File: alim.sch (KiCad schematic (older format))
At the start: 22 parts, among them IC10 74LS138, IC11 74LS138, IC12 74LS139, IC2 74LS09, IC5 74LS123, IC6 74LS393, IC7 74LS14, IC8 74LS04, IC9 74LS11

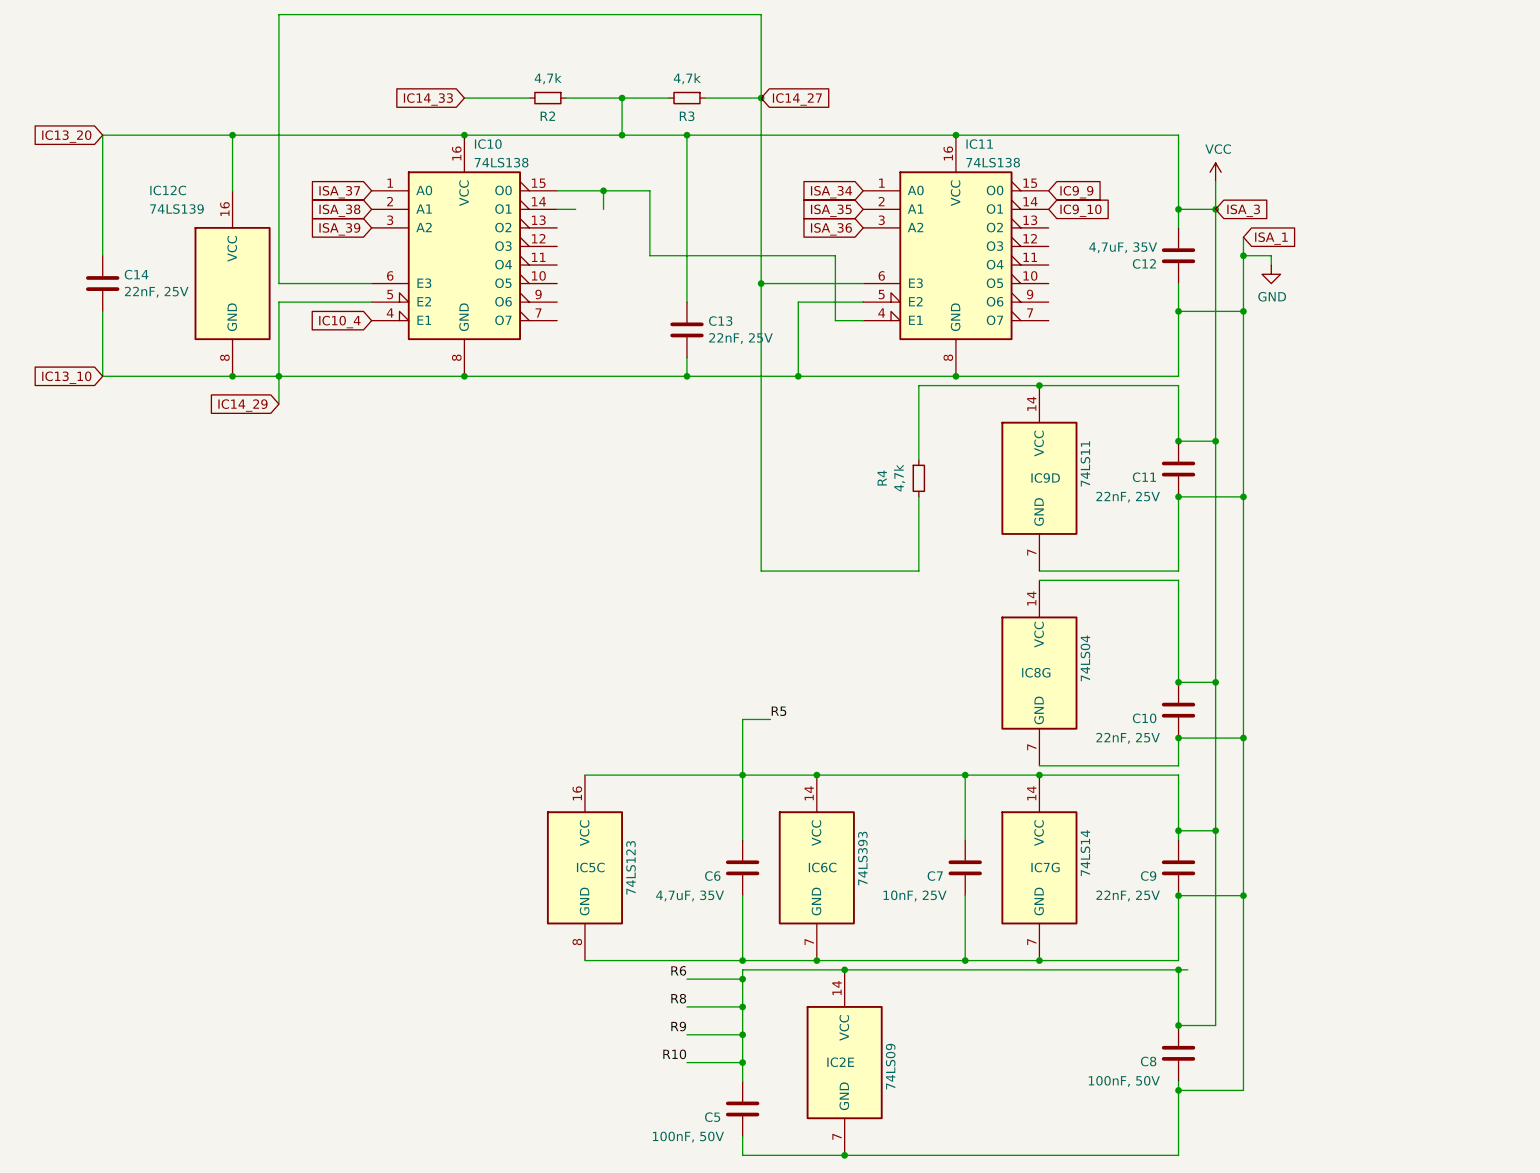
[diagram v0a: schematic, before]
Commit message: modification du bus ISA. ajout de nom sur les pads
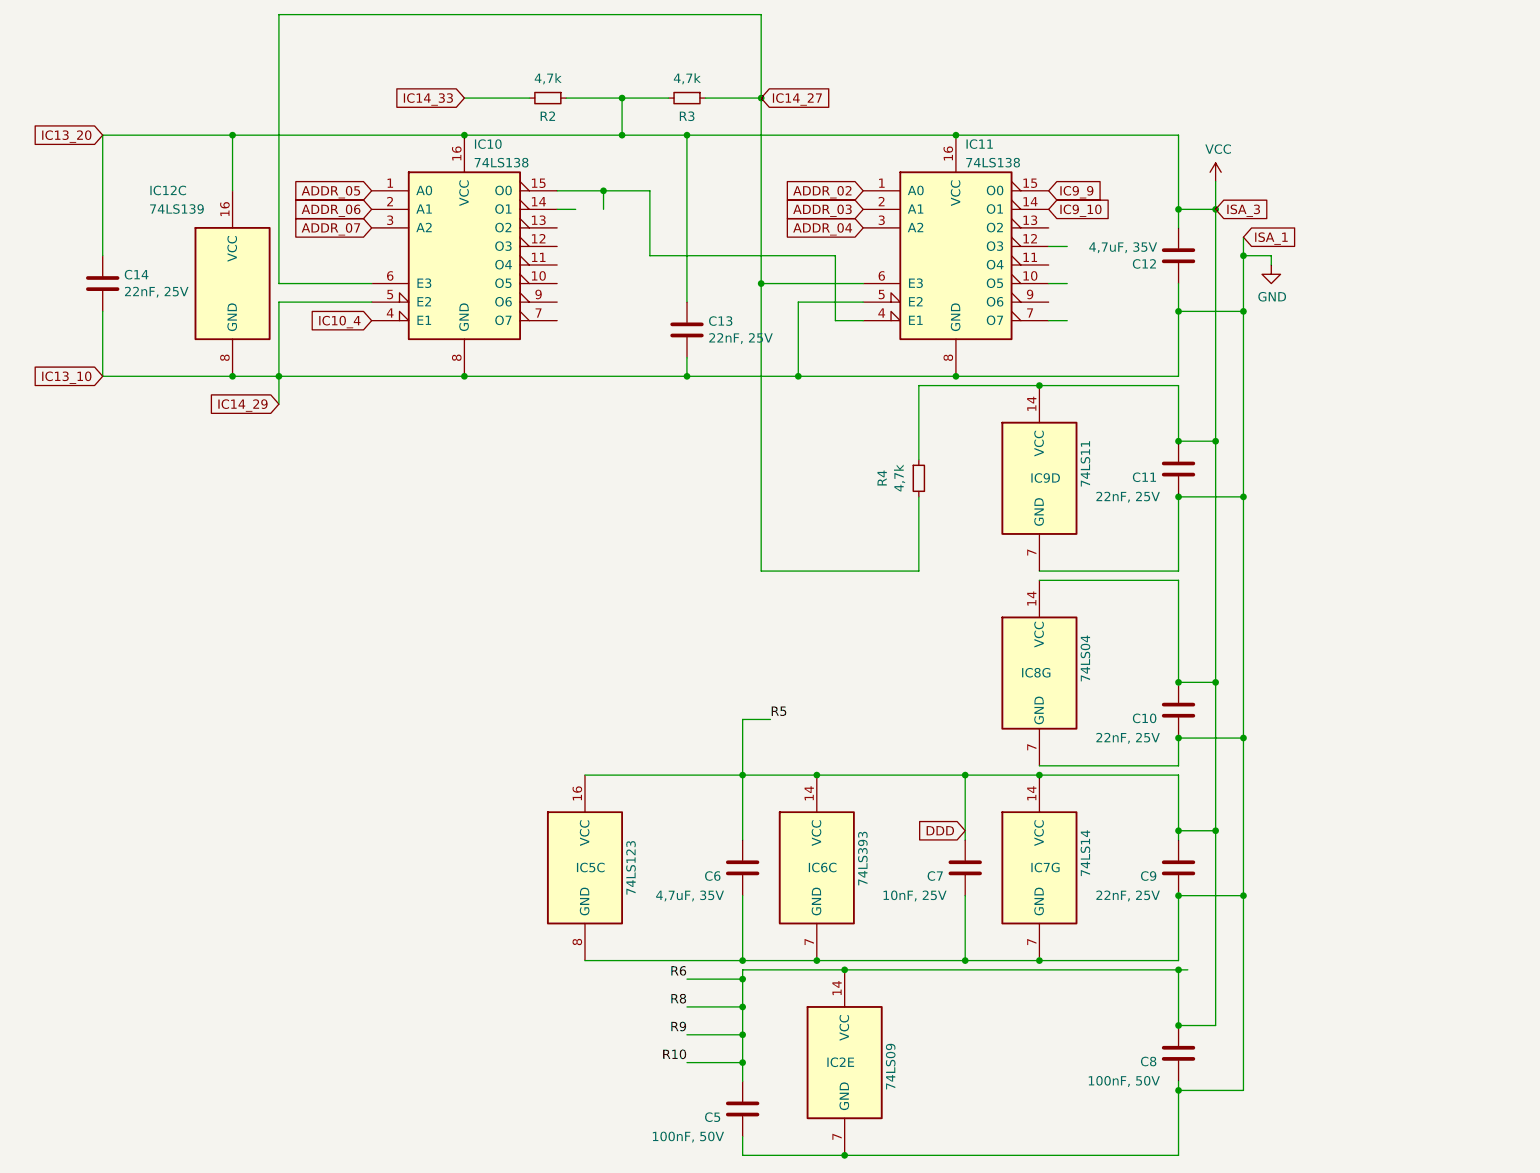
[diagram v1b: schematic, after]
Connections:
- net labels added: ADDR_02, ADDR_03, ADDR_04, ADDR_05, ADDR_06, ADDR_07, DDD
- net labels removed: ISA_34, ISA_35, ISA_36, ISA_37, ISA_38, ISA_39
- wire segments 119 -> 122
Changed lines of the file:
@@
 	4000 2500 4000 2400
 Text GLabel 4950 1700 0    50   Input ~ 0
-ISA_36
+ADDR_04
 Text GLabel 4950 1600 0    50   Input ~ 0
-ISA_35
+ADDR_03
 Text GLabel 4950 1500 0    50   Input ~ 0
-ISA_34
+ADDR_02
 Text GLabel 2300 1700 0    50   Input ~ 0
-ISA_39
+ADDR_07
 Text GLabel 2300 1600 0    50   Input ~ 0
-ISA_38
+ADDR_06
 Text GLabel 2300 1500 0    50   Input ~ 0
-ISA_37
+ADDR_05
 $Comp
 L 74xx:74LS138 IC?
@@
 Wire Wire Line
 	7150 1850 7150 1900
+Text GLabel 5500 4950 0    50   Input ~ 0
+DDD
+Wire Wire Line
+	5950 2000 6050 2000
+Wire Wire Line
+	5950 2200 6050 2200
+Wire Wire Line
+	5950 1800 6050 1800
 $EndSCHEMATC

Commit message: les jumpers
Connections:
- wire segments 122 -> 124
- no-connect marks 0 -> 12
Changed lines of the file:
@@
 AR Path="/61BDF4AD/6132D899" Ref="C12"  Part="1"
 F 0 "C12" H 6765 1896 50  0000 L CNN
-F 1 "4,7uF, 35V" H 6765 1805 50  0000 L CNN
+F 1 "4,7uF, 35V" H 6650 2000 50  0000 L CNN
 F 2 "Capacitor_THT:C_Disc_D4.3mm_W1.9mm_P5.00mm" H 6688 1700 50  0001 C CNN
 F 3 "~" H 6650 1850 50  0001 C CNN
@@
 Wire Wire Line
 	6650 1200 6650 1600
-Text GLabel 5950 1500 2    50   Input ~ 0
+Text GLabel 6100 1500 2    50   Input ~ 0
 IC9_9
 Connection ~ 5450 1200
@@
 Wire Wire Line
 	3550 1500 3800 1500
-Text GLabel 5950 1600 2    50   Input ~ 0
+Text GLabel 6150 1600 2    50   Input ~ 0
 IC9_10
 Wire Wire Line
@@
 Text GLabel 5500 4950 0    50   Input ~ 0
 DDD
-Wire Wire Line
-	5950 2000 6050 2000
-Wire Wire Line
-	5950 2200 6050 2200
-Wire Wire Line
-	5950 1800 6050 1800
+NoConn ~ 5950 2200
+NoConn ~ 5950 2000
+NoConn ~ 5950 1800
+NoConn ~ 6150 1800
+NoConn ~ 6150 2000
+NoConn ~ 6150 2200
+Wire Wire Line
+	6150 1600 6150 2200
+Wire Wire Line
+	5950 1600 6150 1600
+Wire Wire Line
+	6100 1500 6050 1500
+Wire Wire Line
+	6050 1500 6050 2100
+Connection ~ 6050 1500
+Wire Wire Line
+	6050 1500 5950 1500
+NoConn ~ 5950 1700
+NoConn ~ 6050 1700
+NoConn ~ 5950 1900
+NoConn ~ 6050 1900
+NoConn ~ 5950 2100
+NoConn ~ 6050 2100
 $EndSCHEMATC

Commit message: Schema de Freddy
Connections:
- net labels added: A_300-303, A_304-307, A_3xx
- net labels removed: IC10_4, IC13_10, IC13_20, IC14_29, IC9_10, IC9_9
- wire segments 124 -> 113
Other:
- moved on the sheet: R2, R3
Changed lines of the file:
@@
 $Descr A4 11693 8268
 encoding utf-8
-Sheet 3 3
+Sheet 1 1
 Title ""
 Date ""
@@
 L power:GND #PWR?
 U 1 1 612D8F44
-P 7150 1900
-F 0 "#PWR?" H 7150 1650 50  0001 C CNN
-F 1 "GND" H 7155 1727 50  0000 C CNN
-F 2 "" H 7150 1900 50  0001 C CNN
-F 3 "" H 7150 1900 50  0001 C CNN
-	1    7150 1900
+P 3350 2500
+F 0 "#PWR?" H 3350 2250 50  0001 C CNN
+F 1 "GND" H 3355 2327 50  0000 C CNN
+F 2 "" H 3350 2500 50  0001 C CNN
+F 3 "" H 3350 2500 50  0001 C CNN
+	1    3350 2500
 	1    0    0    -1
 $EndComp
@@
 	6650 2850 6850 2850
 Connection ~ 6650 2850
-Text GLabel 7000 1750 2    50   Input ~ 0
+Text GLabel 8150 1750 2    50   Input ~ 0
 ISA_1
-Text GLabel 6850 1600 2    50   Input ~ 0
+Text GLabel 7000 1600 2    50   Input ~ 0
 ISA_3
 $Comp
 L Device:R_Small R?
 U 1 1 6132D869
-P 4000 1000
+P 2600 3450
 AR Path="/6126F7E9/6132D869" Ref="R?"  Part="1"
 AR Path="/61BDF4AD/6132D869" Ref="R3"  Part="1"
-F 0 "R3" V 4100 1000 50  0000 C CNN
-F 1 "4,7k" V 3895 1000 50  0000 C CNN
-F 2 "Resistor_THT:R_Axial_DIN0309_L9.0mm_D3.2mm_P12.70mm_Horizontal" H 4000 1000 50  0001 C CNN
-F 3 "~" H 4000 1000 50  0001 C CNN
-	1    4000 1000
+F 0 "R3" V 2700 3450 50  0000 C CNN
+F 1 "4,7k" V 2495 3450 50  0000 C CNN
+F 2 "Resistor_THT:R_Axial_DIN0309_L9.0mm_D3.2mm_P12.70mm_Horizontal" H 2600 3450 50  0001 C CNN
+F 3 "~" H 2600 3450 50  0001 C CNN
+	1    2600 3450
 	0    1    1    0
 $EndComp
@@
 AR Path="/6126F7E9/6132D88D" Ref="IC?"  Part="1"
 AR Path="/61BDF4AD/6132D88D" Ref="IC11"  Part="1"
+AR Path="/6132D88D" Ref="IC11"  Part="1"
 F 0 "IC11" H 5500 2350 50  0000 L CNN
 F 1 "74LS138" H 5500 2250 50  0000 L CNN
@@
 $EndComp
 Wire Wire Line
-	1550 1500 1550 1200
-Wire Wire Line
 	1800 2000 2300 2000
 Wire Wire Line
@@
 	1800 2500 2800 2500
 Wire Wire Line
-	2800 1200 3650 1200
-Connection ~ 2800 1200
-Connection ~ 3650 1200
-Wire Wire Line
-	4000 1200 4000 2100
-Text GLabel 4400 1000 2    50   Input ~ 0
-IC14_27
+	4000 2000 4000 2100
 Wire Wire Line
 	4850 5700 6650 5700
@@
 Wire Wire Line
 	4850 6700 6650 6700
-Wire Wire Line
-	7150 1850 7000 1850
 Connection ~ 6850 4950
 Wire Wire Line
@@
 Wire Wire Line
 	6650 2000 6650 2150
-Wire Wire Line
-	7000 1850 7000 2150
 Connection ~ 7000 3150
 Connection ~ 6850 2850
 Wire Wire Line
 	6850 1450 6850 1600
-Wire Wire Line
-	6650 1200 6650 1600
-Text GLabel 6100 1500 2    50   Input ~ 0
-IC9_9
-Connection ~ 5450 1200
-Wire Wire Line
-	5450 1200 6650 1200
+Text GLabel 6150 1500 2    50   Output ~ 0
+A_300-303
 Connection ~ 5450 2500
 Wire Wire Line
 	5450 2500 6650 2500
-Wire Wire Line
-	3650 1200 4000 1200
 Wire Wire Line
 	4600 2100 4600 2500
@@
 	4600 2500 5450 2500
 Wire Wire Line
-	4400 2000 4400 1000
-Wire Wire Line
 	5900 2550 5250 2550
 Wire Wire Line
@@
 Wire Wire Line
 	4400 3550 5250 3550
-Connection ~ 4400 2000
-Wire Wire Line
-	4400 2000 4950 2000
 $Comp
 L Device:R_Small R?
 U 1 1 614CCF22
-P 3250 1000
+P 1850 3450
 AR Path="/6126F7E9/614CCF22" Ref="R?"  Part="1"
 AR Path="/61BDF4AD/614CCF22" Ref="R2"  Part="1"
-F 0 "R2" V 3350 1000 50  0000 C CNN
-F 1 "4,7k" V 3145 1000 50  0000 C CNN
-F 2 "Resistor_THT:R_Axial_DIN0309_L9.0mm_D3.2mm_P12.70mm_Horizontal" H 3250 1000 50  0001 C CNN
-F 3 "~" H 3250 1000 50  0001 C CNN
-	1    3250 1000
+F 0 "R2" V 1950 3450 50  0000 C CNN
+F 1 "4,7k" V 1745 3450 50  0000 C CNN
+F 2 "Resistor_THT:R_Axial_DIN0309_L9.0mm_D3.2mm_P12.70mm_Horizontal" H 1850 3450 50  0001 C CNN
+F 3 "~" H 1850 3450 50  0001 C CNN
+	1    1850 3450
 	0    1    1    0
 $EndComp
 Wire Wire Line
 	7000 2150 6650 2150
-Connection ~ 7000 2150
 Wire Wire Line
 	7000 2150 7000 3150
@@
 Wire Wire Line
 	6650 1600 6850 1600
-Connection ~ 6650 1600
 Wire Wire Line
 	6650 1600 6650 1700
@@
 	6850 1600 6850 2850
 Wire Wire Line
-	4100 1000 4400 1000
-Wire Wire Line
-	3900 1000 3650 1000
-Wire Wire Line
-	3650 1000 3650 1200
-Wire Wire Line
-	3650 1000 3350 1000
-Connection ~ 3650 1000
-Text GLabel 2800 1000 0    50   Input ~ 0
+	2500 3450 2250 3450
+Wire Wire Line
+	2250 3450 1950 3450
+Connection ~ 2250 3450
+Text GLabel 1400 3450 0    50   Input ~ 0
 IC14_33
 Wire Wire Line
-	3150 1000 2800 1000
-Wire Wire Line
-	850  1200 850  1850
+	1750 3450 1400 3450
+Wire Wire Line
+	850  1750 850  1850
 Text GLabel 2300 2200 0    50   Input ~ 0
-IC10_4
-Connection ~ 4000 1200
-Wire Wire Line
-	4000 1200 5450 1200
+A_3xx
 Connection ~ 4000 2500
 Wire Wire Line
 	4000 2500 4600 2500
 Wire Wire Line
-	2800 2500 4000 2500
+	2800 2500 3350 2500
 Wire Wire Line
 	3550 1500 3550 1600
@@
 Wire Wire Line
 	3550 1500 3800 1500
-Text GLabel 6150 1600 2    50   Input ~ 0
-IC9_10
+Text GLabel 6150 1600 2    50   Output ~ 0
+A_304-307
 Wire Wire Line
 	7000 6350 6650 6350
@@
 Wire Wire Line
 	850  2500 1550 2500
-Connection ~ 1550 1200
-Wire Wire Line
-	1550 1200 2800 1200
-Wire Wire Line
-	850  1200 1550 1200
-Wire Wire Line
-	1800 2500 1800 2650
-Text GLabel 1800 2650 0    50   Input ~ 0
-IC14_29
-Text GLabel 850  2500 0    50   Input ~ 0
-IC13_10
-Text GLabel 850  1200 0    50   Input ~ 0
-IC13_20
 Wire Wire Line
 	1800 550  4400 550
 Wire Wire Line
-	4400 550  4400 1000
-Wire Wire Line
 	1800 550  1800 2000
-Connection ~ 4400 1000
-Wire Wire Line
-	7000 1750 7000 1850
-Connection ~ 7000 1850
-Wire Wire Line
-	7150 1850 7150 1900
+Wire Wire Line
+	8150 1750 8150 1850
 Text GLabel 5500 4950 0    50   Input ~ 0
 DDD
@@
 	5950 1600 6150 1600
 Wire Wire Line
-	6100 1500 6050 1500
+	6150 1500 6050 1500
 Wire Wire Line
 	6050 1500 6050 2100
@@
 NoConn ~ 5950 2100
 NoConn ~ 6050 2100
+Connection ~ 3350 2500
+Wire Wire Line
+	3350 2500 4000 2500
+$Comp
+L power:GND #PWR?
+U 1 1 61332220
+P 8150 1850
+F 0 "#PWR?" H 8150 1600 50  0001 C CNN
+F 1 "GND" H 8155 1677 50  0000 C CNN
+F 2 "" H 8150 1850 50  0001 C CNN
+F 3 "" H 8150 1850 50  0001 C CNN
+	1    8150 1850
+	1    0    0    -1
+$EndComp
+Wire Wire Line
+	7000 1600 6850 1600
+$Comp
+L power:VCC #PWR?
+U 1 1 6134655A
+P 5450 1200
+F 0 "#PWR?" H 5450 1050 50  0001 C CNN
+F 1 "VCC" H 5465 1373 50  0000 C CNN
+F 2 "" H 5450 1200 50  0001 C CNN
+F 3 "" H 5450 1200 50  0001 C CNN
+	1    5450 1200
+	1    0    0    -1
+$EndComp
+$Comp
+L power:VCC #PWR?
+U 1 1 6134C22C
+P 2250 3350
+F 0 "#PWR?" H 2250 3200 50  0001 C CNN
+F 1 "VCC" H 2265 3523 50  0000 C CNN
+F 2 "" H 2250 3350 50  0001 C CNN
+F 3 "" H 2250 3350 50  0001 C CNN
+	1    2250 3350
+	1    0    0    -1
+$EndComp
+Wire Wire Line
+	2250 3350 2250 3450
+$Comp
+L power:VCC #PWR?
+U 1 1 61355045
+P 4000 2000
+F 0 "#PWR?" H 4000 1850 50  0001 C CNN
+F 1 "VCC" H 4015 2173 50  0000 C CNN
+F 2 "" H 4000 2000 50  0001 C CNN
+F 3 "" H 4000 2000 50  0001 C CNN
+	1    4000 2000
+	1    0    0    -1
+$EndComp
+$Comp
+L power:VCC #PWR?
+U 1 1 61356035
+P 2800 1200
+F 0 "#PWR?" H 2800 1050 50  0001 C CNN
+F 1 "VCC" H 2815 1373 50  0000 C CNN
+F 2 "" H 2800 1200 50  0001 C CNN
+F 3 "" H 2800 1200 50  0001 C CNN
+	1    2800 1200
+	1    0    0    -1
+$EndComp
+Text GLabel 3150 3450 2    50   Input ~ 0
+IC14_27
+Wire Wire Line
+	3150 3450 2700 3450
+Wire Wire Line
+	4400 550  4400 2000
+Connection ~ 4400 2000
+Wire Wire Line
+	4400 2000 4950 2000
+$Comp
+L power:VCC #PWR?
+U 1 1 6137A5D8
+P 1550 1500
+F 0 "#PWR?" H 1550 1350 50  0001 C CNN
+F 1 "VCC" H 1565 1673 50  0000 C CNN
+F 2 "" H 1550 1500 50  0001 C CNN
+F 3 "" H 1550 1500 50  0001 C CNN
+	1    1550 1500
+	1    0    0    -1
+$EndComp
+$Comp
+L power:VCC #PWR?
+U 1 1 6137B0FA
+P 850 1750
+F 0 "#PWR?" H 850 1600 50  0001 C CNN
+F 1 "VCC" H 865 1923 50  0000 C CNN
+F 2 "" H 850 1750 50  0001 C CNN
+F 3 "" H 850 1750 50  0001 C CNN
+	1    850  1750
+	1    0    0    -1
+$EndComp
 $EndSCHEMATC

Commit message: Dernière version de Freddy
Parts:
- removed C13: 22nF, 25V, Capacitor_THT:C_Disc_D4.3mm_W1.9mm_P5.00mm, symbol Device:C
- removed IC10, IC11: 74LS138, Package_DIP:DIP-16_W7.62mm, symbol 74xx:74LS138
- removed R4: 4,7k, Resistor_THT:R_Axial_DIN0309_L9.0mm_D3.2mm_P12.70mm_Horizontal, symbol Device:R_Small
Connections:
- net labels removed: ADDR_02, ADDR_03, ADDR_04, ADDR_05, ADDR_06, ADDR_07, A_300-303, A_304-307, A_3xx, DDD, ISA_1, ISA_3, R10, R5, R6, R8, R9
- wire segments 113 -> 49
- no-connect marks 12 -> 0
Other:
- note added: "Next to ISA 3"
- moved on the sheet: C10, C11, C12, C5, C6, C7, C8, C9, IC2E, IC5C, IC6C, IC7G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
